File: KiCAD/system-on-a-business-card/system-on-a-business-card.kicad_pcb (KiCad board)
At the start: 2 copper layers, 85 x 55 mm, 105 parts, among them J1 USB_C_Receptacle, J2 X077-6428TSWCG01-H13, Q1 2N7002K, Q10 2N7002K, Q11 2N7002K, Q12 2N7002K, Q2 BSS84, Q3 2N7002K, Q4 2N7002K, Q5 2N7002K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

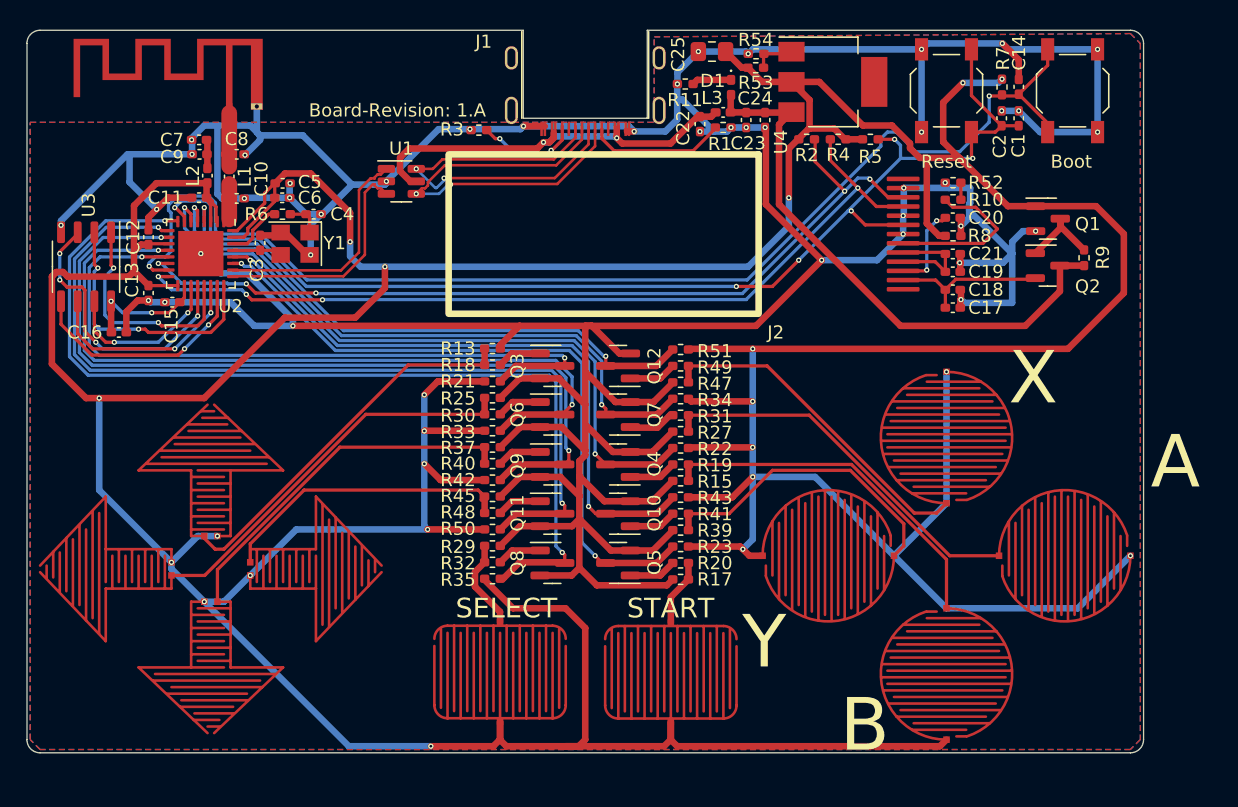
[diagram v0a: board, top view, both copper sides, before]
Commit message: minor tweaks in design, added thermal relief vias
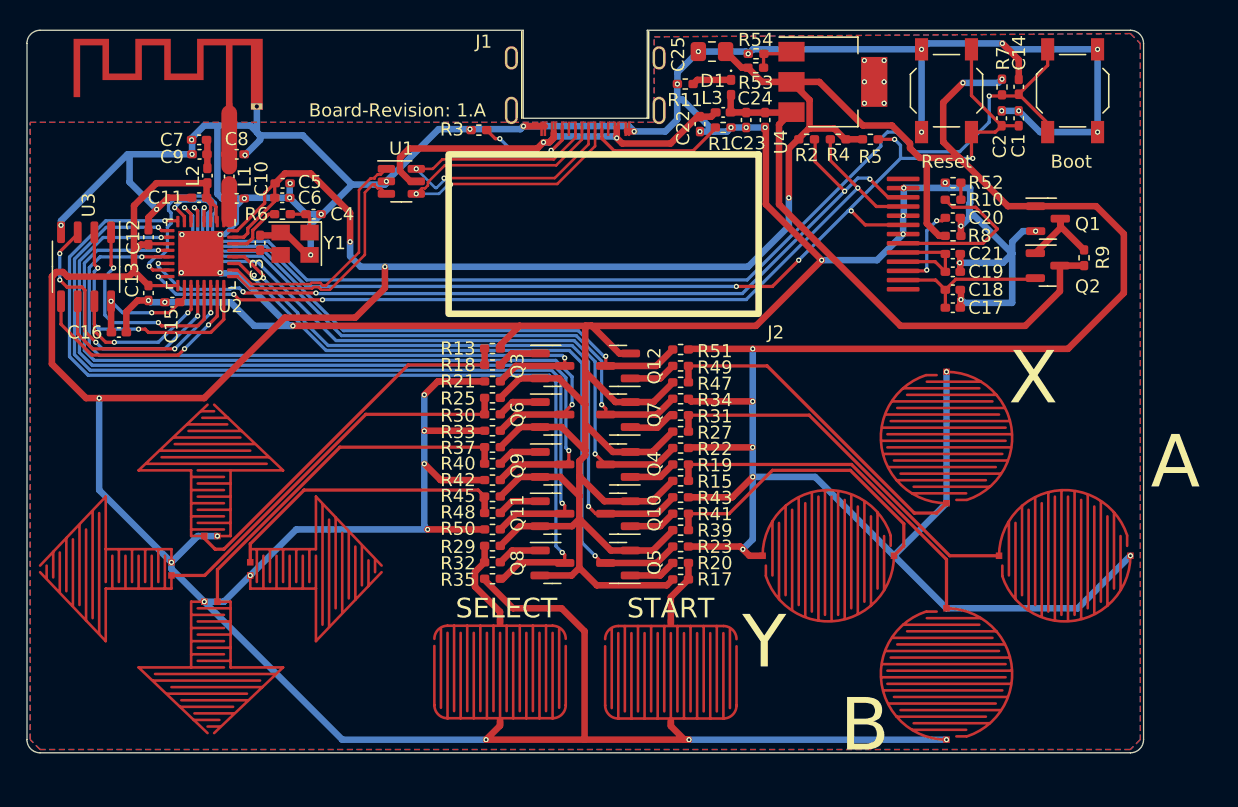
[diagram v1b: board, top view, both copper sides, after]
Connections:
- U4 pad 4: unconnected-(U4-Pad4) -> GND
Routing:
- net +3.3V: track 479.9 -> 475.2 mm, vias 22 -> 24
- net GND: track 389.3 -> 390.7 mm, vias 41 -> 50
- net USB_D+: track 17.7 -> 18.7 mm
- net USB_D-: track 17.7 -> 18.6 mm
- net /Host/PAD_B: track 52.0 -> 52.9 mm
- net /Host/PAD_X: track 43.8 -> 44.7 mm
- net /Host/PAD_A: track 47.8 -> 48.7 mm
- net RESET: track 90.5 -> 91.2 mm

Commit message: updated documentation, fixed bom export
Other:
- board text added: "Board-Revision: 1.0.0"
- board text removed: "Board-Revision: 1.A"
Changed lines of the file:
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@@
     (property "Sheetfile" "display_circuit.kicad_sch")
     (property "Sheetname" "Display Circuit")
-    (property "exclude_from_bom" "")
-    (attr smd exclude_from_bom)
+    (attr smd)
     (fp_text reference "J2" (at 1.3 13.55 unlocked) (layer "F.SilkS")
       (effects (font (size 1 1) (thickness 0.15)))
@@
     (effects (font (size 1.5 1.5) (thickness 0.15)))
   )
-  (gr_text "Board-Revision: 1.A" (at 105.7 76.1) (layer "F.SilkS")
+  (gr_text "Board-Revision: 1.0.0" (at 105.15 76.15) (layer "F.SilkS")
     (effects (font (size 1 1) (thickness 0.15)))
   )
@@
     (effects (font (size 4 4) (thickness 0.15)))
   )
-  (gr_text "QR Code generated here: https://goqr.me/#t=url\nsvg scaling 0.4" (at 80 95) (layer "Margin")
+  (gr_text "QR Code generated here: https://goqr.me/#t=url\nsvg scaling 0.4" (at 80 95) (layer "Cmts.User")
     (effects (font (size 1 1) (thickness 0.15)) (justify left))
   )
-  (gr_text "QR Code generated here: https://goqr.me/#t=vcard\nsvg scaling 0.375" (at 159 91) (layer "Margin")
+  (gr_text "QR Code generated here: https://goqr.me/#t=vcard\nsvg scaling 0.375" (at 159 91) (layer "Cmts.User")
     (effects (font (size 1 1) (thickness 0.15)) (justify right))
   )

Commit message: fixed #12 connected OLED VDD pins to 3.3V power line
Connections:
- C19 pad 1: Net-(C19-Pad1) -> +3.3V
- C21 pad 1: Net-(C19-Pad1) -> +3.3V
- J2 pad 4: Net-(C19-Pad1) -> +3.3V
- J2 pad 5: Net-(C19-Pad1) -> +3.3V
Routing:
- net +3.3V: track 475.2 -> 498.4 mm
- net Net-(C19-Pad1): track 7.97 -> 0.00 mm

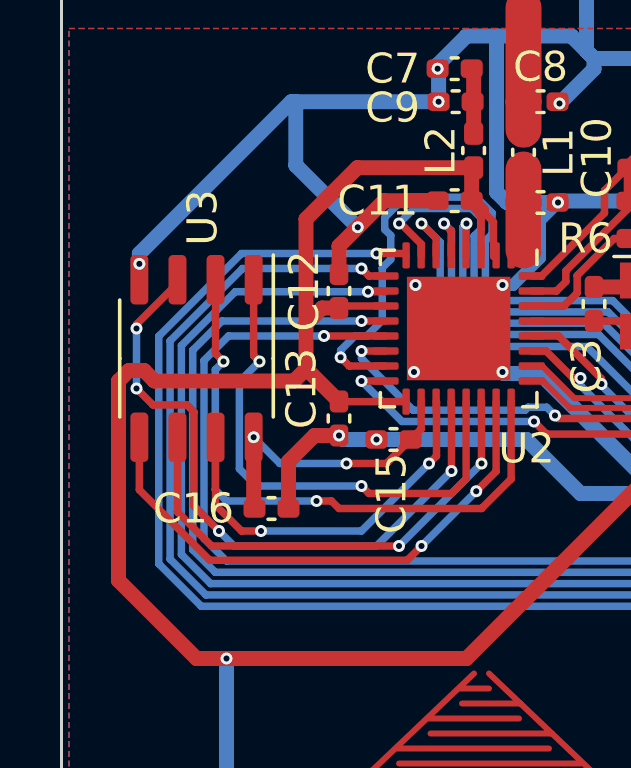
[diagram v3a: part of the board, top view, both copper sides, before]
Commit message: fixes #11: Footprint of Flash IC corrected
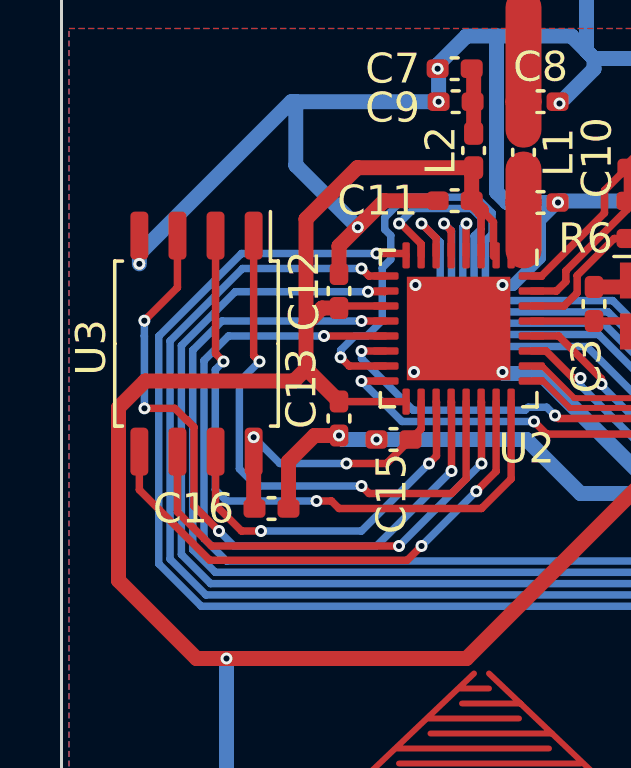
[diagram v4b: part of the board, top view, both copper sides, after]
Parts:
- U3: footprint Package_SO:SOP-8_3.9x4.9mm_P1.27mm -> Package_SO:SOP-8_5.28x5.23mm_P1.27mm
- moved U3 0.50 mm to (82.0, 87.5)
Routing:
- net Net-(U2-SPIQ/GPIO17): track 20.3 -> 21.3 mm
- net Net-(U2-SPIHD/GPIO12): track 12.8 -> 11.9 mm
- net Net-(U2-SPID/GPIO16): track 18.2 -> 17.2 mm
- net Net-(U2-SPICS0/GPIO14): track 17.3 -> 18.3 mm
- net Net-(U2-SPICLK/GPIO15): track 16.3 -> 15.3 mm
- net Net-(U2-SPIWP/GPIO13): track 21.9 -> 22.8 mm
- net +3.3V: track 498.4 -> 497.6 mm

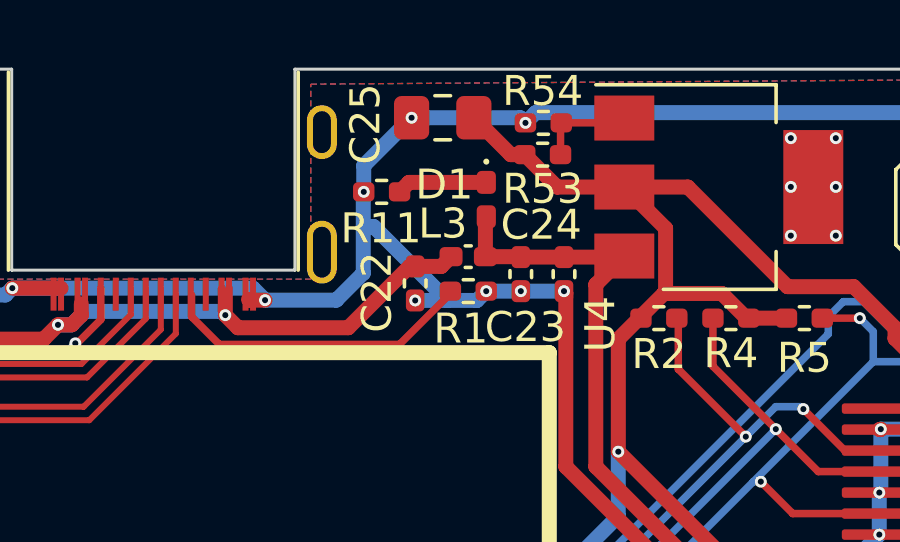
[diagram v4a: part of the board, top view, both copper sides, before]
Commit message: fixes #15: moved wire to connecting D1 from L3 to C24
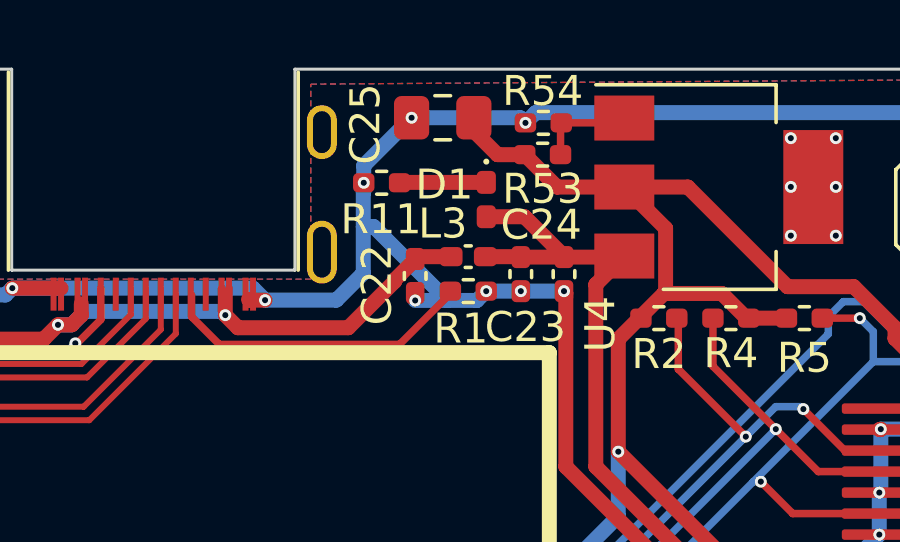
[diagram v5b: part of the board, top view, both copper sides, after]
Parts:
- moved R11 0.30 mm to (127.6, 73.8)
- moved C22 0.25 mm to (128.7, 76.9)
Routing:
- net +5V: track 43.4 -> 45.3 mm
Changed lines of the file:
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@@
   )
   (footprint "Capacitor_SMD:C_0402_1005Metric_Pad0.74x0.62mm_HandSolder" (layer "F.Cu")
-    (at 128.73 77.1425 -90)
+    (at 128.73 76.8945 -90)
     (descr "Capacitor SMD 0402 (1005 Metric), square (rectangular) end terminal, IPC_7351 nominal with elongated pad for handsoldering. (Body size source: IPC-SM-782 page 76, https://www.pcb-3d.com/wordpress/wp-content/uploads/ipc-sm-782a_amendment_1_and_2.pdf), generated with kicad-footprint-generator")
     (tags "capacitor handsolder")
@@
   )
   (footprint "Resistor_SMD:R_0402_1005Metric_Pad0.72x0.64mm_HandSolder" (layer "F.Cu")
-    (at 127.6125 74.09 180)
+    (at 127.6125 73.787 180)
     (descr "Resistor SMD 0402 (1005 Metric), square (rectangular) end terminal, IPC_7351 nominal with elongated pad for handsoldering. (Body size source: IPC-SM-782 page 72, https://www.pcb-3d.com/wordpress/wp-content/uploads/ipc-sm-782a_amendment_1_and_2.pdf), generated with kicad-footprint-generator")
     (tags "resistor handsolder")
@@
   (via (at 132.405 71.79) (size 0.4) (drill 0.2) (layers "F.Cu" "B.Cu") (net 1))
   (via (at 99.9 84) (size 0.4) (drill 0.2) (layers "F.Cu" "B.Cu") (net 1))
-  (via (at 127.015 74.09) (size 0.4) (drill 0.2) (layers "F.Cu" "B.Cu") (net 1))
+  (via (at 127.015 73.787) (size 0.4) (drill 0.2) (layers "F.Cu" "B.Cu") (net 1))
   (via (at 147.4 81.6) (size 0.4) (drill 0.2) (layers "F.Cu" "B.Cu") (net 1))
   (via (at 148.5975 84.9025) (size 0.4) (drill 0.2) (layers "F.Cu" "B.Cu") (net 1))
@@
   (segment (start 135.7 73.93) (end 137.82 73.93) (width 0.5) (layer "F.Cu") (net 5))
   (segment (start 147.2875 86.9) (end 144.215 86.9) (width 0.25) (layer "F.Cu") (net 5))
-  (segment (start 131.915 72.85) (end 130.685 71.62) (width 0.5) (layer "F.Cu") (net 5))
   (segment (start 144.723 78.624471) (end 144.723 78.977) (width 0.5) (layer "F.Cu") (net 5))
   (segment (start 128.0575 98.25) (end 127.8575 98.05) (width 0.5) (layer "F.Cu") (net 5))
@@
   (segment (start 107.766075 100.483925) (end 112.34 100.483925) (width 0.5) (layer "F.Cu") (net 5))
   (segment (start 91.1725 82.74) (end 91.5 83.0675) (width 0.5) (layer "F.Cu") (net 5))
+  (segment (start 132.38 72.85) (end 131.4732 72.85) (width 0.5) (layer "F.Cu") (net 5))
   (segment (start 114.5 114) (end 118.2 114) (width 0.5) (layer "F.Cu") (net 5))
   (segment (start 131.2 105.55) (end 132.75 104) (width 0.5) (layer "F.Cu") (net 5))
@@
   (segment (start 94 85.75) (end 94.311 85.439) (width 0.25) (layer "F.Cu") (net 5))
   (segment (start 91 98) (end 83 98) (width 0.5) (layer "F.Cu") (net 5))
-  (segment (start 132.38 72.85) (end 131.915 72.85) (width 0.5) (layer "F.Cu") (net 5))
   (segment (start 131.8 109.3) (end 132 109.5) (width 0.5) (layer "F.Cu") (net 5))
   (segment (start 135.5 82.75) (end 135.5 79) (width 0.5) (layer "F.Cu") (net 5))
@@
   (segment (start 146 84.708098) (end 146 79.714759) (width 0.5) (layer "F.Cu") (net 5))
   (segment (start 79.4 95.4) (end 79.4 89.637) (width 0.5) (layer "F.Cu") (net 5))
+  (segment (start 131.4732 72.85) (end 130.685 72.0618) (width 0.5) (layer "F.Cu") (net 5))
+  (segment (start 130.685 72.0618) (end 130.685 71.62) (width 0.5) (layer "F.Cu") (net 5))
   (segment (start 140.38 87.63) (end 144.185 87.63) (width 0.5) (layer "F.Cu") (net 5))
   (segment (start 147.25 78.5) (end 148.75 80) (width 0.5) (layer "F.Cu") (net 5))
@@
   (segment (start 146.6725 89.015) (end 147.4125 89.755) (width 0.25) (layer "F.Cu") (net 11))
   (segment (start 116.823 78.523) (end 117.277 78.523) (width 0.5) (layer "F.Cu") (net 12))
-  (segment (start 122.82 78.62) (end 126.5 78.62) (width 0.5) (layer "F.Cu") (net 12))
   (segment (start 117.6 78.2) (end 117.6 77.823) (width 0.5) (layer "F.Cu") (net 12))
+  (segment (start 126.5 78.62) (end 128.043 77.077) (width 0.5) (layer "F.Cu") (net 12))
   (segment (start 117.277 78.523) (end 117.6 78.2) (width 0.5) (layer "F.Cu") (net 12))
   (segment (start 122.275 78.075) (end 122.275 77.3) (width 0.25) (layer "F.Cu") (net 12))
-  (segment (start 126.5 78.62) (end 128.545 76.575) (width 0.5) (layer "F.Cu") (net 12))
+  (segment (start 128.043 77.077) (end 128.043 77.029138) (width 0.5) (layer "F.Cu") (net 12))
   (segment (start 122.525 78.325) (end 122.275 78.075) (width 0.25) (layer "F.Cu") (net 12))
-  (segment (start 129.6 76.575) (end 129.925 76.25) (width 0.5) (layer "F.Cu") (net 12))
-  (segment (start 122.4 78.2) (end 122.82 78.62) (width 0.5) (layer "F.Cu") (net 12))
-  (segment (start 128.73 76.575) (end 129.6 76.575) (width 0.5) (layer "F.Cu") (net 12))
-  (segment (start 128.545 76.575) (end 128.73 76.575) (width 0.5) (layer "F.Cu") (net 12))
+  (segment (start 128.043 77.029138) (end 128.821338 76.2508) (width 0.5) (layer "F.Cu") (net 12))
+  (segment (start 128.821338 76.2508) (end 129.7718 76.2508) (width 0.5) (layer "F.Cu") (net 12))
+  (segment (start 122.82 78.62) (end 126.5 78.62) (width 0.5) (layer "F.Cu") (net 12))
   (segment (start 122.525 77.3) (end 122.525 78.325) (width 0.25) (layer "F.Cu") (net 12))
   (segment (start 116.823 78.523) (end 116.346 79) (width 0.5) (layer "F.Cu") (net 12))
@@
   (segment (start 105.902 80.722291) (end 106.679709 81.5) (width 0.5) (layer "F.Cu") (net 12))
   (segment (start 105.902 79.698) (end 105.902 80.722291) (width 0.5) (layer "F.Cu") (net 12))
+  (segment (start 122.4 78.2) (end 122.82 78.62) (width 0.5) (layer "F.Cu") (net 12))
   (segment (start 106.6 79) (end 105.902 79.698) (width 0.5) (layer "F.Cu") (net 12))
   (segment (start 106.679709 81.5) (end 107.1375 81.5) (width 0.5) (layer "F.Cu") (net 12))
@@
   (segment (start 116.823 78.523) (end 117.277 78.523) (width 0.5) (layer "B.Cu") (net 12))
   (segment (start 131.07 76.25) (end 132.235 76.25) (width 0.5) (layer "F.Cu") (net 13))
+  (segment (start 133.69 76.265) (end 133.69 76.2352) (width 0.5) (layer "F.Cu") (net 13))
   (segment (start 133.69 76.265) (end 135.665 76.265) (width 0.5) (layer "F.Cu") (net 13))
-  (segment (start 131.07 76.25) (end 131.07 74.95) (width 0.5) (layer "F.Cu") (net 13))
+  (segment (start 132.3748 74.92) (end 131.1 74.92) (width 0.5) (layer "F.Cu") (net 13))
   (segment (start 153.5 92.5) (end 156.135 89.865) (width 0.5) (layer "F.Cu") (net 13))
   (segment (start 156.135 87.915) (end 157.9725 87.915) (width 0.5) (layer "F.Cu") (net 13))
@@
   (segment (start 144 92.5) (end 153.5 92.5) (width 0.5) (layer "F.Cu") (net 13))
   (segment (start 135.7 76.23) (end 134.75 77.18) (width 0.5) (layer "F.Cu") (net 13))
+  (segment (start 133.69 76.2352) (end 132.3748 74.92) (width 0.5) (layer "F.Cu") (net 13))
   (segment (start 134.75 83.25) (end 144 92.5) (width 0.5) (layer "F.Cu") (net 13))
   (segment (start 122.2 79.175) (end 121.275 78.25) (width 0.25) (layer "F.Cu") (net 14))
@@
   (segment (start 146 85.25) (end 146.75 84.5) (width 0.25) (layer "B.Cu") (net 16))
   (segment (start 146 88.25) (end 146 85.25) (width 0.25) (layer "B.Cu") (net 16))
-  (segment (start 128.525 73.775) (end 128.21 74.09) (width 0.5) (layer "F.Cu") (net 17))
   (segment (start 131.1 73.775) (end 128.525 73.775) (width 0.5) (layer "F.Cu") (net 17))
   (segment (start 138.655 79.905) (end 140.75 82) (width 0.25) (layer "F.Cu") (net 18))

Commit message: resolves #13: changed resistor for LED from 121R to 47k to reduce brightness significantly
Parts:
- R11: value 121R -> 47k
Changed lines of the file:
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@@
         (effects (font (size 1 1) (thickness 0.15)))
     )
-    (fp_text value "121R" (at 0 1.17) (layer "F.Fab")
+    (fp_text value "47k" (at 0 1.17) (layer "F.Fab")
         (effects (font (size 1 1) (thickness 0.15)))
     )

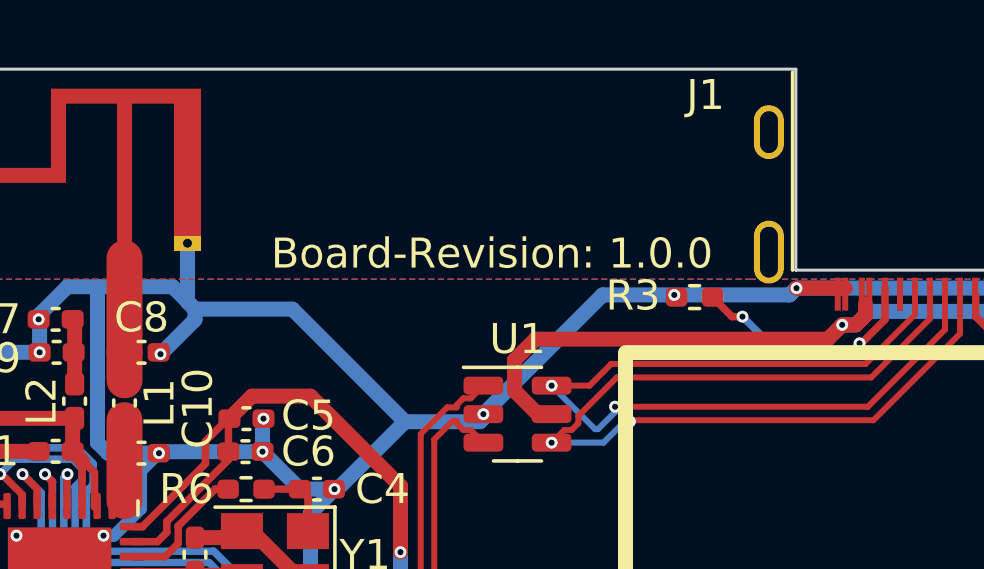
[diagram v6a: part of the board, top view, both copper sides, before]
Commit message: Updated documentation and production files
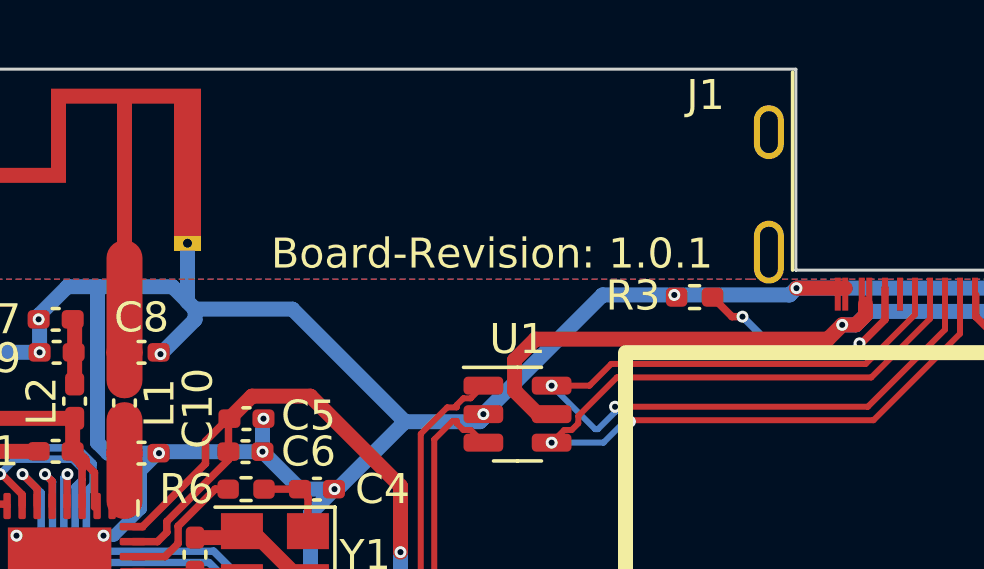
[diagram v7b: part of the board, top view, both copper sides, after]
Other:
- board text added: "Board-Revision: 1.0.1"
- board text removed: "Board-Revision: 1.0.0"
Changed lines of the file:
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@@
     (effects (font (size 1.5 1.5) (thickness 0.15)))
   )
-  (gr_text "Board-Revision: 1.0.0" (at 105.15 76.15) (layer "F.SilkS")
+  (gr_text "Board-Revision: 1.0.1" (at 105.15 76.15) (layer "F.SilkS")
     (effects (font (size 1 1) (thickness 0.15)))
   )
